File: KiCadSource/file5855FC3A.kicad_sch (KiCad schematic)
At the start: 20 parts, among them U31 DAC5662

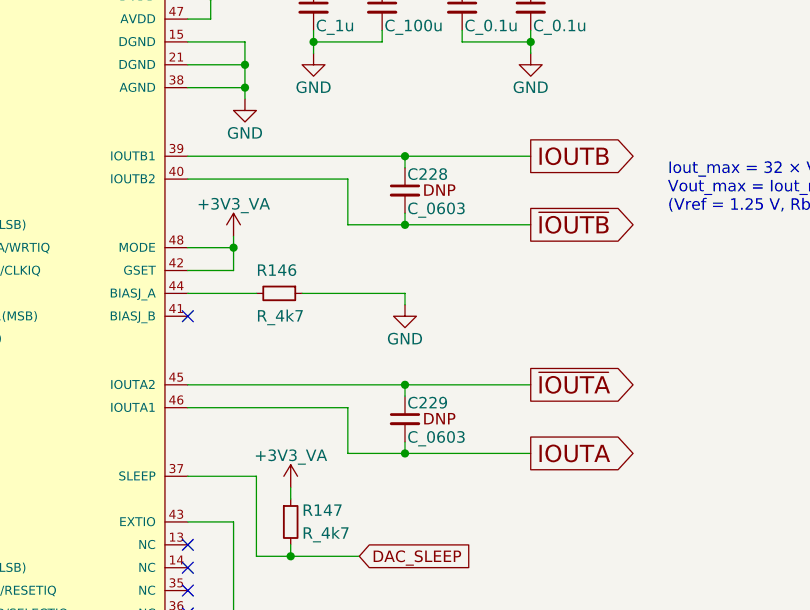
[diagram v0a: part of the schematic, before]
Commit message: updating part attributes
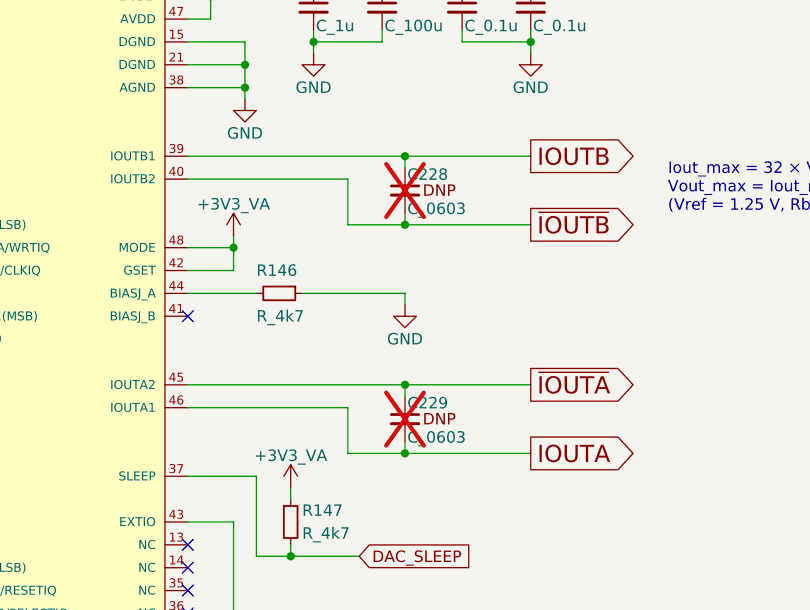
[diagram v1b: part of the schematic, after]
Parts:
- C228, C229: now not fitted
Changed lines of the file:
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@@
 		(in_bom yes)
 		(on_board yes)
-		(dnp no)
+		(dnp yes)
 		(property "Reference" "C228"
 			(at 159.004 64.262 0)
@@
 		(in_bom yes)
 		(on_board yes)
-		(dnp no)
+		(dnp yes)
 		(property "Reference" "C229"
 			(at 159.004 89.662 0)
